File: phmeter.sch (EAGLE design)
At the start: 2 parts, among them IC1 FT232BL, U1 328P

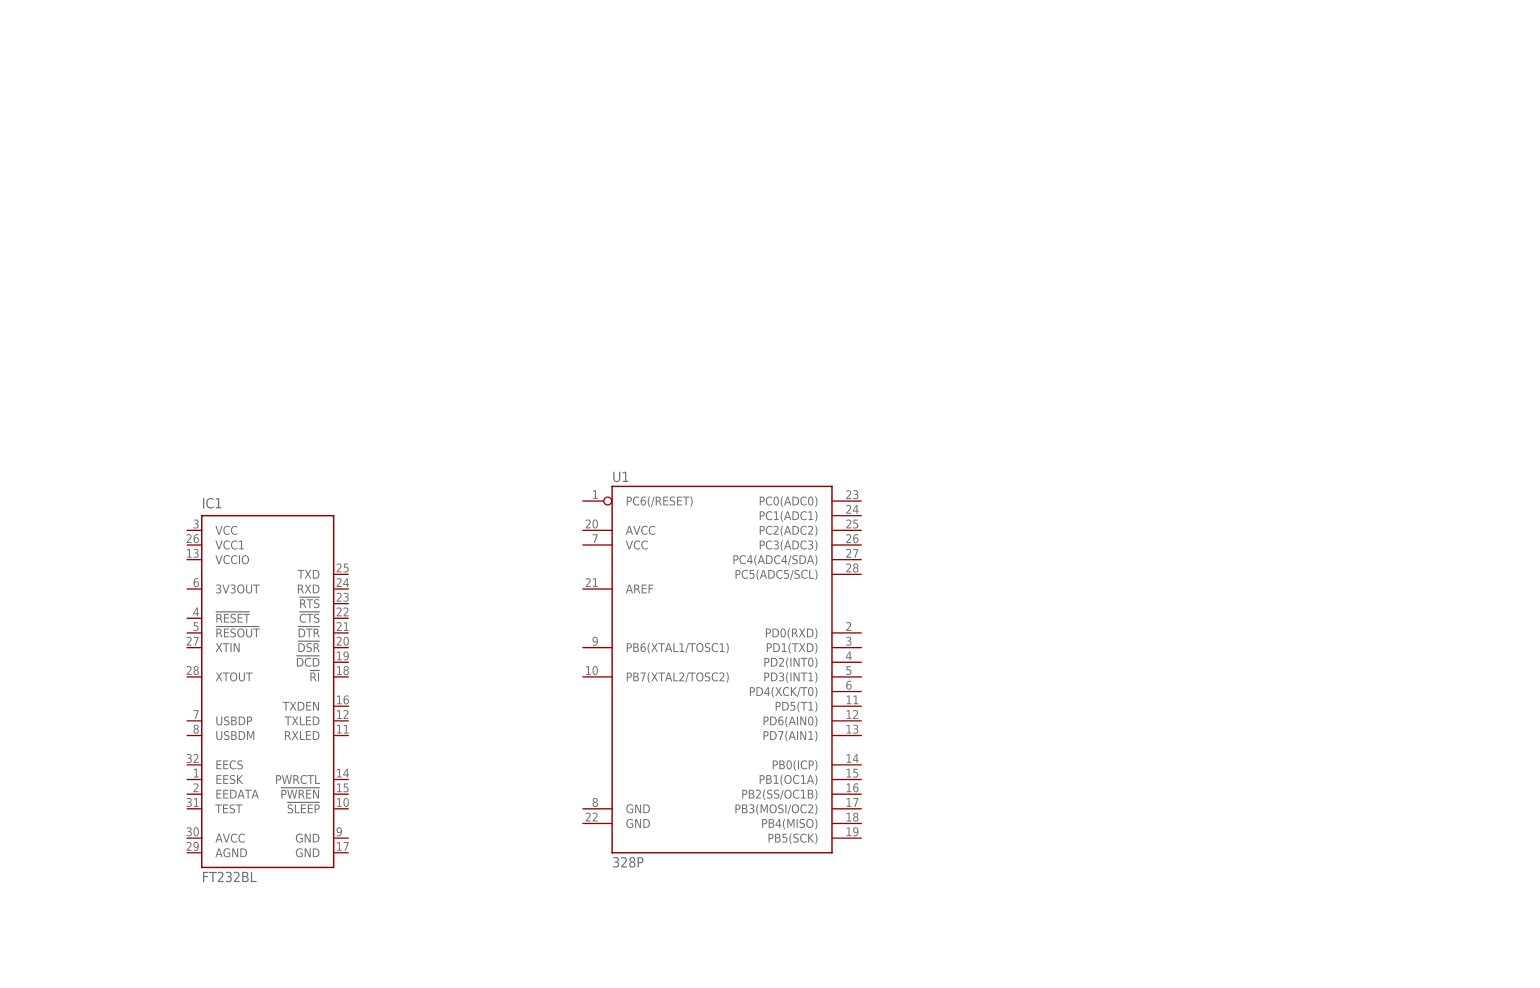
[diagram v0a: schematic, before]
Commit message: LCD - ADC Working - updated PCB
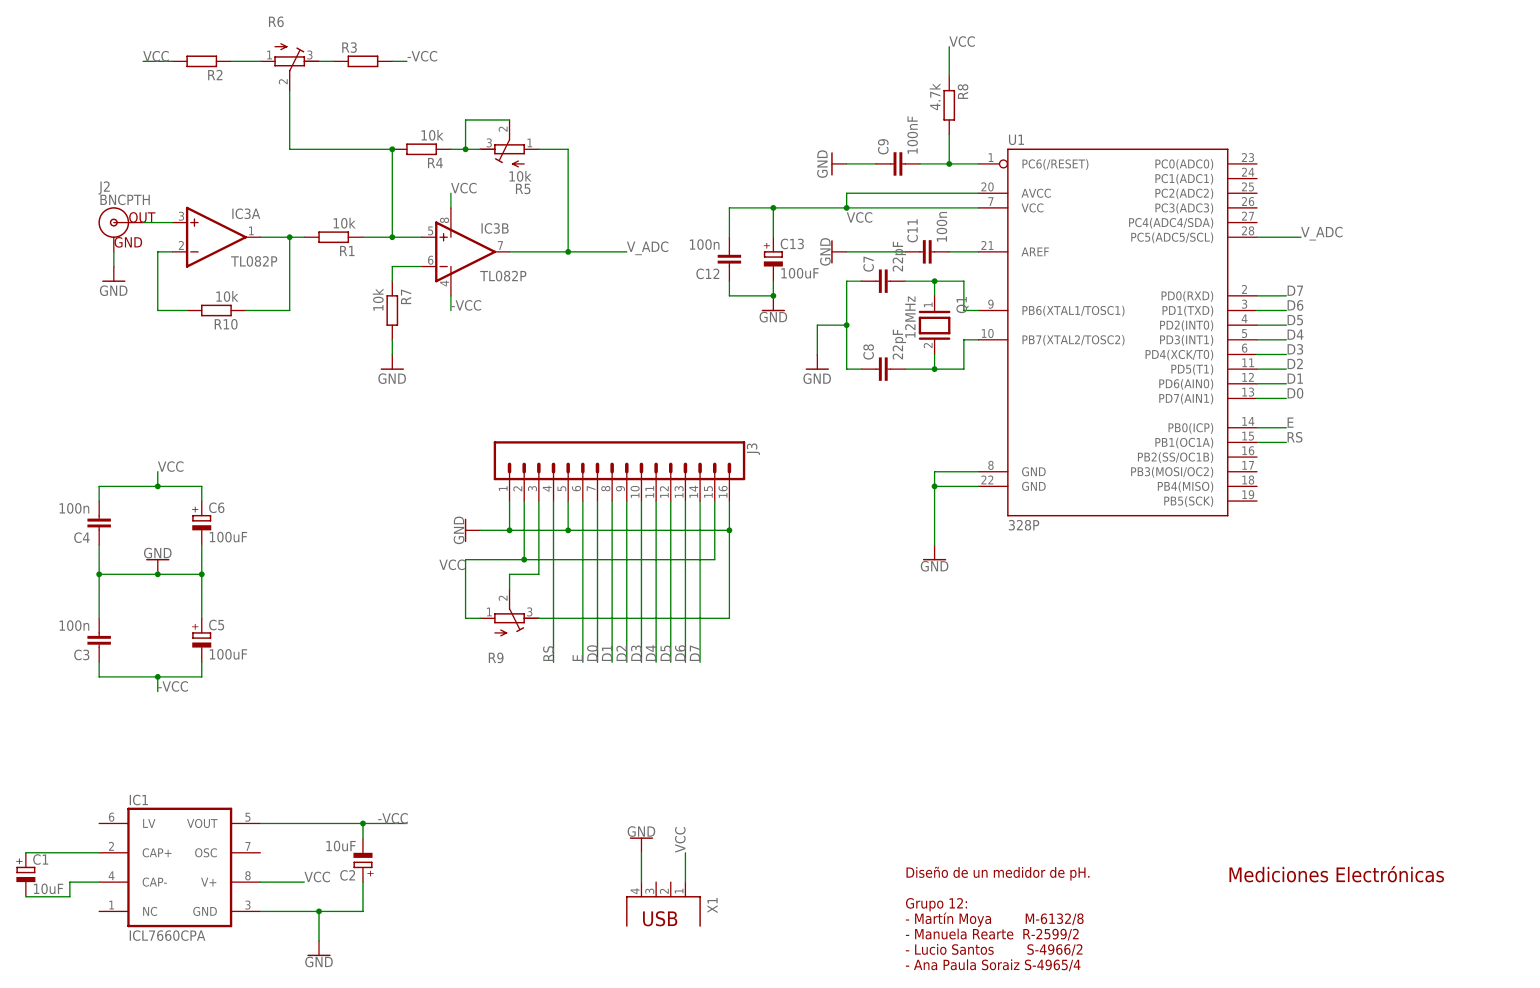
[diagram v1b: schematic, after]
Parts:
- added C1, C2: 10uF, rcl:CPOL-EUE1.8-4
- added C11, C12, C3, C4: 100n, resistor:C-EU025-024X044
- added C13, C5, C6: 100uF, rcl:CPOL-EUE1.8-4
- added C7, C8: 22pF, resistor:C-EU025-024X044
- added C9: 100nF, resistor:C-EU025-024X044
- added IC3: TL082P, linear:TL082P
- added J2: BNCPTH, SparkFun-Connectors:BNCPTH
- added J3: (no value), SparkFun-Connectors:CONN_16
- added Q1: 12MHz, special:XTAL/S
- added R1, R10, R4, R7: 10k, rcl:R-EU_0207/10
- added R2, R3: (no value), rcl:R-EU_0207/10
- added R5: 10k, rcl:R-TRIMM64W
- added R6, R9: (no value), rcl:R-TRIMM64W
- added R8: 4.7k, rcl:R-EU_0207/10
- added X1: (no value), con-berg:PN61729
- IC1: value FT232BL -> ICL7660CPA; device ftdichip:FT232BL -> maxim:ICL7660CPA
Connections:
- new net -VCC: C2.-, C3.1, C5.-, IC1.VOUT, IC3P.V-, R3.2
- new net D0: J3.7, U1.PD7(AIN1)
- new net D1: J3.8, U1.PD6(AIN0)
- new net D2: J3.9, U1.PD5(T1)
- new net D3: J3.10, U1.PD4(XCK/T0)
- new net D4: J3.11, U1.PD3(INT1)
- new net D5: J3.12, U1.PD2(INT0)
- new net D6: J3.13, U1.PD1(TXD)
- new net D7: J3.14, U1.PD0(RXD)
- new net E: J3.6, U1.PB0(ICP)
- new net GND: C11.1, C12.1, C13.-, C2.+, C3.2, C4.1, C5.+, C6.-, C7.1, C8.1, C9.1, IC1.GND, J2.GND, J3.1, J3.16, J3.5, R7.2, R9.E, U1.GND@1, U1.GND@2, X1.4
- new net N$1: IC3A.OUT, R1.2, R10.1
- new net N$10: J3.3, R9.S
- new net N$11: C11.2, U1.AREF
- new net N$12: C9.2, R8.2, U1.PC6(/RESET)
- new net N$2: C1.+, IC1.CAP+
- new net N$22: IC3A.+IN, J2.OUT
- new net N$23: IC3A.-IN, R10.2
- new net N$3: R4.1, R5.E, R5.S
- new net N$4: IC3B.-IN, R7.1
- new net N$5: C1.-, IC1.CAP-
- new net N$6: R3.1, R6.E
- new net N$7: R2.1, R6.A
- new net N$8: C7.2, Q1.1, U1.PB6(XTAL1/TOSC1)
- new net N$9: C8.2, Q1.2, U1.PB7(XTAL2/TOSC2)
- new net RS: J3.4, U1.PB1(OC1A)
- new net VCC: C12.2, C13.+, C4.2, C6.+, IC1.V+, IC3P.V+, J3.15, J3.2, R2.2, R8.1, R9.A, U1.AVCC, U1.VCC, X1.1
- new net V_ADC: IC3B.OUT, R5.A, U1.PC5(ADC5/SCL)
- new net V_OFFSET: IC3B.+IN, R1.1, R4.2, R6.S
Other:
- note added: "Diseño de un medidor de pH. Grupo 12: - Martín Moya M-6132/8 - Manuela Rearte R-2599/2 - Lucio Santos S-4966/2 - Ana Paula Soraiz S-4965/4"
- note added: "Mediciones Electrónicas"
- moved on the sheet: U1

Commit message: Finished Board Design
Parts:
- removed C9: 100nF, resistor:C-EU025-024X044
- renumbered R5 to GAIN, R6 to OFFSET
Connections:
- net GND: no longer C9.1
- net N$12: no longer C9.2
- net V_ADC: now also U1.PC1(ADC1); no longer U1.PC5(ADC5/SCL)
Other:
- moved on the sheet: R8
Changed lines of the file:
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@@
 <part name="R3" library="rcl" library_urn="urn:adsk.eagle:library:334" deviceset="R-EU_" device="0207/10" package3d_urn="urn:adsk.eagle:package:23491/1"/>
 <part name="R4" library="rcl" library_urn="urn:adsk.eagle:library:334" deviceset="R-EU_" device="0207/10" package3d_urn="urn:adsk.eagle:package:23491/1" value="10k"/>
-<part name="R5" library="rcl" library_urn="urn:adsk.eagle:library:334" deviceset="R-TRIMM" device="64W" package3d_urn="urn:adsk.eagle:package:23748/1" value="10k"/>
-<part name="R6" library="rcl" library_urn="urn:adsk.eagle:library:334" deviceset="R-TRIMM" device="64W" package3d_urn="urn:adsk.eagle:package:23748/1"/>
+<part name="GAIN" library="rcl" library_urn="urn:adsk.eagle:library:334" deviceset="R-TRIMM" device="64W" package3d_urn="urn:adsk.eagle:package:23748/1" value="10k"/>
+<part name="OFFSET" library="rcl" library_urn="urn:adsk.eagle:library:334" deviceset="R-TRIMM" device="64W" package3d_urn="urn:adsk.eagle:package:23748/1"/>
 <part name="R7" library="rcl" library_urn="urn:adsk.eagle:library:334" deviceset="R-EU_" device="0207/10" package3d_urn="urn:adsk.eagle:package:23491/1" value="10k"/>
 <part name="GND2" library="supply1" library_urn="urn:adsk.eagle:library:371" deviceset="GND" device=""/>
@@
 <part name="C8" library="resistor" library_urn="urn:adsk.eagle:library:348" deviceset="C-EU" device="025-024X044" package3d_urn="urn:adsk.eagle:package:26149/1" value="22pF"/>
 <part name="GND6" library="supply1" library_urn="urn:adsk.eagle:library:371" deviceset="GND" device=""/>
-<part name="C9" library="resistor" library_urn="urn:adsk.eagle:library:348" deviceset="C-EU" device="025-024X044" package3d_urn="urn:adsk.eagle:package:26149/1" value="100nF"/>
 <part name="R8" library="rcl" library_urn="urn:adsk.eagle:library:334" deviceset="R-EU_" device="0207/10" package3d_urn="urn:adsk.eagle:package:23491/1" value="4.7k"/>
-<part name="GND7" library="supply1" library_urn="urn:adsk.eagle:library:371" deviceset="GND" device=""/>
 <part name="GND8" library="SparkFun-PowerSymbols" library_urn="urn:adsk.eagle:library:530" deviceset="GND" device=""/>
 <part name="GND9" library="SparkFun-PowerSymbols" library_urn="urn:adsk.eagle:library:530" deviceset="GND" device=""/>
@@
 <instance part="R3" gate="G$1" x="68.58" y="162.56"/>
 <instance part="R4" gate="G$1" x="78.74" y="147.32" rot="R180"/>
-<instance part="R5" gate="G$1" x="93.98" y="147.32" rot="R90"/>
-<instance part="R6" gate="G$1" x="55.88" y="162.56" rot="R270"/>
+<instance part="GAIN" gate="G$1" x="93.98" y="147.32" rot="R90"/>
+<instance part="OFFSET" gate="G$1" x="55.88" y="162.56" rot="R270"/>
 <instance part="R7" gate="G$1" x="73.66" y="119.38" rot="R270"/>
 <instance part="GND2" gate="1" x="73.66" y="109.22"/>
@@
 <instance part="C8" gate="G$1" x="157.48" y="109.22" rot="R90"/>
 <instance part="GND6" gate="1" x="147.32" y="109.22"/>
-<instance part="C9" gate="G$1" x="160.02" y="144.78" rot="R90"/>
-<instance part="R8" gate="G$1" x="170.18" y="154.94" rot="R270"/>
-<instance part="GND7" gate="1" x="149.86" y="144.78" rot="MR90"/>
+<instance part="R8" gate="G$1" x="165.1" y="144.78"/>
 <instance part="GND8" gate="1" x="139.7" y="119.38"/>
 <instance part="GND9" gate="1" x="86.36" y="81.28" rot="R270"/>
@@
 </segment>
 <segment>
-<pinref part="GND7" gate="1" pin="GND"/>
-<pinref part="C9" gate="G$1" pin="1"/>
-<wire x1="152.4" y1="144.78" x2="157.48" y2="144.78" width="0.1524" layer="91"/>
-</segment>
-<segment>
 <pinref part="GND8" gate="1" pin="GND"/>
 <wire x1="139.7" y1="124.46" x2="139.7" y2="121.92" width="0.1524" layer="91"/>
@@
 <segment>
 <pinref part="R4" gate="G$1" pin="1"/>
-<pinref part="R5" gate="G$1" pin="E"/>
+<pinref part="GAIN" gate="G$1" pin="E"/>
 <wire x1="83.82" y1="147.32" x2="86.36" y2="147.32" width="0.1524" layer="91"/>
-<pinref part="R5" gate="G$1" pin="S"/>
+<pinref part="GAIN" gate="G$1" pin="S"/>
 <wire x1="86.36" y1="147.32" x2="88.9" y2="147.32" width="0.1524" layer="91"/>
 <wire x1="93.98" y1="152.4" x2="86.36" y2="152.4" width="0.1524" layer="91"/>
@@
 <net name="V_ADC" class="0">
 <segment>
-<pinref part="R5" gate="G$1" pin="A"/>
+<pinref part="GAIN" gate="G$1" pin="A"/>
 <wire x1="99.06" y1="147.32" x2="104.14" y2="147.32" width="0.1524" layer="91"/>
 <wire x1="104.14" y1="147.32" x2="104.14" y2="129.54" width="0.1524" layer="91"/>
@@
 </segment>
 <segment>
-<pinref part="U1" gate="G$1" pin="PC5(ADC5/SCL)"/>
-<wire x1="223.52" y1="132.08" x2="231.14" y2="132.08" width="0.1524" layer="91"/>
-<label x="231.14" y="132.08" size="1.778" layer="95"/>
+<pinref part="U1" gate="G$1" pin="PC1(ADC1)"/>
+<wire x1="223.52" y1="142.24" x2="233.68" y2="142.24" width="0.1524" layer="91"/>
+<label x="233.68" y="142.24" size="1.778" layer="95"/>
 </segment>
 </net>
@@
 <segment>
 <pinref part="R3" gate="G$1" pin="1"/>
-<pinref part="R6" gate="G$1" pin="E"/>
+<pinref part="OFFSET" gate="G$1" pin="E"/>
 <wire x1="63.5" y1="162.56" x2="60.96" y2="162.56" width="0.1524" layer="91"/>
 </segment>
@@
 <net name="N$7" class="0">
 <segment>
-<pinref part="R6" gate="G$1" pin="A"/>
+<pinref part="OFFSET" gate="G$1" pin="A"/>
 <pinref part="R2" gate="G$1" pin="1"/>
 <wire x1="50.8" y1="162.56" x2="45.72" y2="162.56" width="0.1524" layer="91"/>
@@
 <wire x1="73.66" y1="147.32" x2="55.88" y2="147.32" width="0.1524" layer="91"/>
 <junction x="73.66" y="147.32"/>
-<pinref part="R6" gate="G$1" pin="S"/>
+<pinref part="OFFSET" gate="G$1" pin="S"/>
 <wire x1="55.88" y1="147.32" x2="55.88" y2="157.48" width="0.1524" layer="91"/>
 </segment>
@@
 <net name="N$12" class="0">
 <segment>
-<pinref part="C9" gate="G$1" pin="2"/>
 <pinref part="U1" gate="G$1" pin="PC6(/RESET)"/>
-<wire x1="165.1" y1="144.78" x2="170.18" y2="144.78" width="0.1524" layer="91"/>
 <pinref part="R8" gate="G$1" pin="2"/>
 <wire x1="170.18" y1="144.78" x2="175.26" y2="144.78" width="0.1524" layer="91"/>
-<wire x1="170.18" y1="149.86" x2="170.18" y2="144.78" width="0.1524" layer="91"/>
-<junction x="170.18" y="144.78"/>
 </segment>
 </net>
@@
 <segment>
 <pinref part="R8" gate="G$1" pin="1"/>
-<wire x1="170.18" y1="165.1" x2="170.18" y2="160.02" width="0.1524" layer="91"/>
-<label x="170.18" y="165.1" size="1.778" layer="95"/>
-</segment>
-<segment>
+<wire x1="154.94" y1="144.78" x2="160.02" y2="144.78" width="0.1524" layer="91"/>
+<label x="154.94" y="144.78" size="1.778" layer="95"/>
+</segment>
+<segment>
